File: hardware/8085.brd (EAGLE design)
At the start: 167.9 x 122.5 mm, 52 parts, among them IC10 74HCT00N, IC11 74HCT245DW, IC2 74AC573N, IC3 ATF16V8BP3, IC4 74AC00D, IC5 74HCT245DW, IC6 74AC273N, IC7 74HCT139N, IC8 7404N, IC9 74HCT138N

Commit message: Yet another HW issue fixed:
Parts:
- moved R8 3.59 mm to (20.3, 24.8)
- moved R10 2.84 mm to (20.3, 27.3)
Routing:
- net GND: track 131.1 -> 139.4 mm, vias 12 -> 14
- net N$11: track 25.9 -> 20.8 mm
- net N$13: track 18.7 -> 19.3 mm
- net VCC: track 639.6 -> 640.2 mm
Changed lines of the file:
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@@
 </element>
 <element name="R7" library="rcl" package="0207/10" value="" x="56.515" y="30.0736" rot="MR180"/>
-<element name="R8" library="rcl" package="0207/10" value="" x="17.78" y="27.305" rot="R180"/>
-<element name="R10" library="rcl" package="0207/10" value="" x="19.05" y="24.765" rot="R180"/>
+<element name="R8" library="rcl" package="0207/10" value="" x="20.32" y="24.765" rot="R180"/>
+<element name="R10" library="rcl" package="0207/10" value="" x="20.32" y="27.305" rot="R180"/>
 <element name="R11" library="rcl" package="0207/10" value="" x="56.515" y="27.6225" rot="MR180"/>
 <element name="RN1" library="resistor-sil" package="SIL5" value="" x="35.56" y="53.975" rot="R270">
@@
 <wire x1="43.18" y1="37.1983" x2="45.085" y2="37.1983" width="0.6096" layer="16"/>
 <wire x1="45.085" y1="37.1983" x2="47.625" y2="37.1983" width="0.6096" layer="16"/>
-<wire x1="13.97" y1="26.035" x2="12.7" y2="27.305" width="1.016" layer="16"/>
 <wire x1="16.51" y1="36.195" x2="12.7" y2="36.195" width="1.016" layer="16"/>
-<wire x1="13.97" y1="24.765" x2="13.97" y2="26.035" width="1.016" layer="16"/>
-<wire x1="12.7" y1="27.305" x2="12.7" y2="31.115" width="1.016" layer="16"/>
 <wire x1="12.7" y1="31.115" x2="12.7" y2="36.195" width="1.016" layer="16"/>
 <wire x1="4.445" y1="43.815" x2="4.445" y2="41.275" width="1.016" layer="16"/>
@@
 <wire x1="60.325" y1="33.655" x2="61.595" y2="32.385" width="0.4064" layer="16"/>
 <wire x1="61.595" y1="32.385" x2="61.595" y2="30.0736" width="0.4064" layer="16"/>
+<wire x1="12.7" y1="31.115" x2="12.7" y2="29.845" width="1.016" layer="16"/>
+<wire x1="12.7" y1="29.845" x2="15.24" y2="27.305" width="1.016" layer="16"/>
+<wire x1="15.24" y1="24.765" x2="15.24" y2="27.305" width="1.016" layer="16"/>
 </signal>
 <signal name="GND">
@@
 <contactref element="C7" pad="2"/>
 <contactref element="C8" pad="1"/>
-<wire x1="29.21" y1="21.32" x2="40.005" y2="21.32" width="0" layer="19" extent="16-16"/>
+<via x="72.0725" y="19.05" extent="1-16" drill="0.6" diameter="1.4224" shape="octagon"/>
+<via x="72.0725" y="10.795" extent="1-16" drill="0.6" diameter="1.4224" shape="octagon"/>
+<wire x1="72.0725" y1="10.795" x2="72.0725" y2="19.05" width="0.6096" layer="1"/>
 </signal>
 <signal name="D0">
@@
 <wire x1="77.47" y1="19.685" x2="75.565" y2="19.685" width="0.4064" layer="16"/>
 <wire x1="75.565" y1="19.685" x2="67.6275" y2="11.7475" width="0.4064" layer="16"/>
-<wire x1="67.6275" y1="11.7475" x2="25.0825" y2="11.7475" width="0.4064" layer="16"/>
-<wire x1="25.0825" y1="11.7475" x2="21.59" y2="15.24" width="0.4064" layer="16"/>
-<wire x1="21.59" y1="15.24" x2="21.59" y2="38.735" width="0.4064" layer="16"/>
+<wire x1="67.6275" y1="11.7475" x2="24.4475" y2="11.7475" width="0.4064" layer="16"/>
+<wire x1="24.4475" y1="11.7475" x2="21.59" y2="14.605" width="0.4064" layer="16"/>
+<wire x1="21.59" y1="14.605" x2="21.59" y2="38.735" width="0.4064" layer="16"/>
 <via x="21.59" y="38.735" extent="1-16" drill="0.6" diameter="1.4224" shape="octagon"/>
 <wire x1="21.59" y1="38.735" x2="21.59" y2="56.515" width="0.4064" layer="1"/>
@@
 <wire x1="77.47" y1="17.145" x2="74.295" y2="17.145" width="0.4064" layer="16"/>
 <wire x1="74.295" y1="17.145" x2="67.945" y2="10.795" width="0.4064" layer="16"/>
-<wire x1="67.945" y1="10.795" x2="24.765" y2="10.795" width="0.4064" layer="16"/>
-<wire x1="24.765" y1="10.795" x2="20.32" y2="15.24" width="0.4064" layer="16"/>
-<wire x1="20.32" y1="15.24" x2="20.32" y2="40.005" width="0.4064" layer="16"/>
+<wire x1="67.945" y1="10.795" x2="24.13" y2="10.795" width="0.4064" layer="16"/>
+<wire x1="24.13" y1="10.795" x2="20.32" y2="14.605" width="0.4064" layer="16"/>
+<wire x1="20.32" y1="14.605" x2="20.32" y2="40.005" width="0.4064" layer="16"/>
 <via x="20.32" y="40.005" extent="1-16" drill="0.6" diameter="1.4224" shape="octagon"/>
 <wire x1="20.32" y1="40.005" x2="20.32" y2="59.055" width="0.4064" layer="1"/>
@@
 <wire x1="77.47" y1="14.605" x2="73.025" y2="14.605" width="0.4064" layer="16"/>
 <wire x1="73.025" y1="14.605" x2="68.2625" y2="9.8425" width="0.4064" layer="16"/>
-<wire x1="68.2625" y1="9.8425" x2="24.4475" y2="9.8425" width="0.4064" layer="16"/>
-<wire x1="24.4475" y1="9.8425" x2="19.05" y2="15.24" width="0.4064" layer="16"/>
-<wire x1="19.05" y1="15.24" x2="19.05" y2="38.735" width="0.4064" layer="16"/>
+<wire x1="68.2625" y1="9.8425" x2="23.8125" y2="9.8425" width="0.4064" layer="16"/>
+<wire x1="23.8125" y1="9.8425" x2="19.05" y2="14.605" width="0.4064" layer="16"/>
+<wire x1="19.05" y1="14.605" x2="19.05" y2="38.735" width="0.4064" layer="16"/>
 <via x="19.05" y="38.735" extent="1-16" drill="0.6" diameter="1.4224" shape="octagon"/>
 <wire x1="19.05" y1="38.735" x2="19.05" y2="51.435" width="0.4064" layer="1"/>
@@
 <contactref element="CON1" pad="44"/>
 <contactref element="R8" pad="1"/>
-<wire x1="22.86" y1="27.305" x2="22.86" y2="19.685" width="0.4064" layer="16"/>
-<wire x1="22.86" y1="19.685" x2="25.4" y2="17.145" width="0.4064" layer="16"/>
-<wire x1="25.4" y1="17.145" x2="35.2425" y2="17.145" width="0.4064" layer="16"/>
+<wire x1="25.4" y1="24.765" x2="25.4" y2="19.685" width="0.4064" layer="16"/>
+<wire x1="25.4" y1="19.685" x2="27.94" y2="17.145" width="0.4064" layer="16"/>
+<wire x1="27.94" y1="17.145" x2="35.2425" y2="17.145" width="0.4064" layer="16"/>
 <wire x1="35.2425" y1="17.145" x2="36.83" y2="18.7325" width="0.4064" layer="16"/>
 <wire x1="36.83" y1="18.7325" x2="36.83" y2="21.32" width="0.4064" layer="16"/>
@@
 <wire x1="34.29" y1="21.32" x2="34.29" y2="18.7325" width="0.4064" layer="16"/>
 <wire x1="34.29" y1="18.7325" x2="33.655" y2="18.0975" width="0.4064" layer="16"/>
-<wire x1="33.655" y1="18.0975" x2="25.7175" y2="18.0975" width="0.4064" layer="16"/>
-<wire x1="25.7175" y1="18.0975" x2="24.13" y2="19.685" width="0.4064" layer="16"/>
-<wire x1="24.13" y1="19.685" x2="24.13" y2="24.765" width="0.4064" layer="16"/>
+<wire x1="33.655" y1="18.0975" x2="28.2575" y2="18.0975" width="0.4064" layer="16"/>
+<wire x1="28.2575" y1="18.0975" x2="26.67" y2="19.685" width="0.4064" layer="16"/>
+<wire x1="26.67" y1="19.685" x2="26.67" y2="26.035" width="0.4064" layer="16"/>
+<wire x1="26.67" y1="26.035" x2="25.4" y2="27.305" width="0.4064" layer="16"/>
 </signal>
 <signal name="CF_CS0">

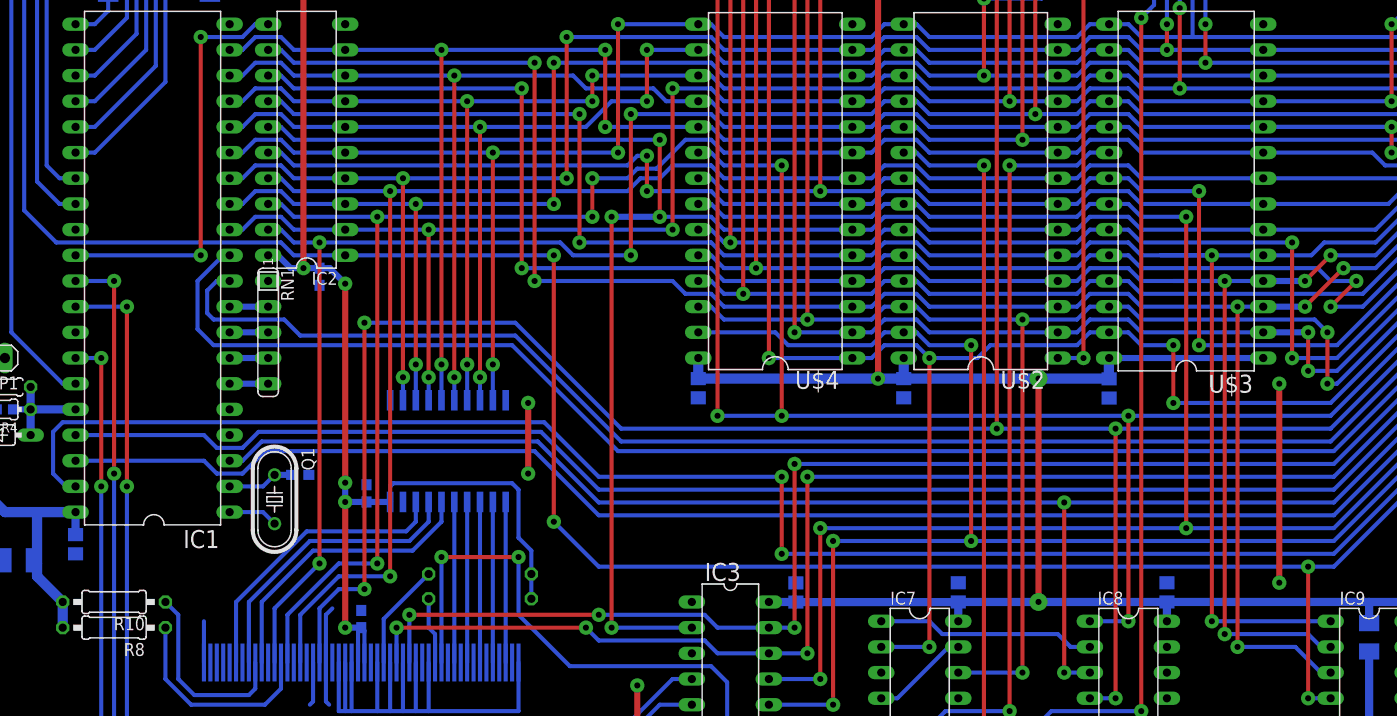
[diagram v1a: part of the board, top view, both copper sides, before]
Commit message: Bug in PCB design fixed
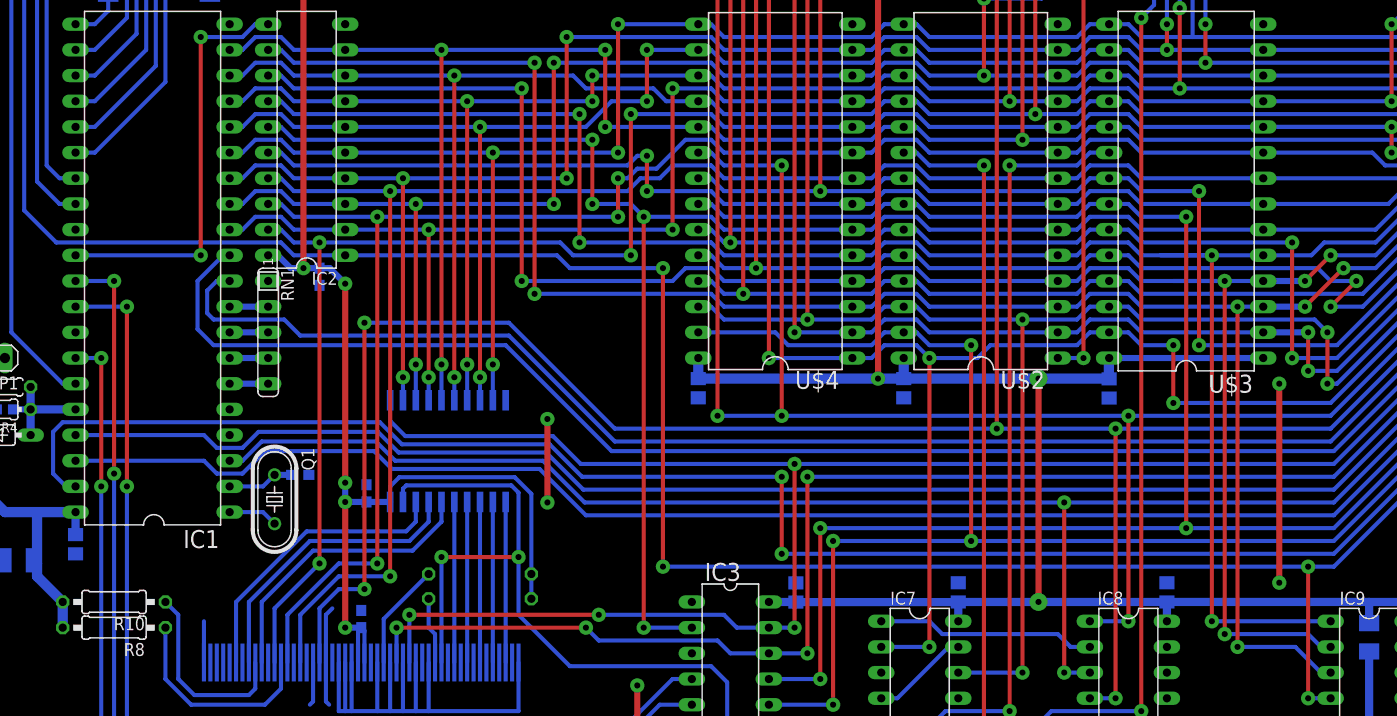
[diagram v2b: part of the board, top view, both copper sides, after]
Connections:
- net CF_CS0: now also IC11.19
- net GND: now also IC3.3, IC3.8, IC3.9
- net IO_RD: now also IC11.1
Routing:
- net IO_RD: track 135.9 -> 179.7 mm
- net CF_CS0: track 57.7 -> 77.2 mm
- net A4: track 187.8 -> 179.1 mm
- net AEN: track 237.3 -> 239.2 mm
- net A6: track 196.7 -> 198.5 mm
- net GND: track 139.4 -> 140.7 mm
- net VCC: track 640.2 -> 641.1 mm
- net A7: track 197.5 -> 198.3 mm
